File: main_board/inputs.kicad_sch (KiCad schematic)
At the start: 35 parts, among them J16 3.5mm Jack, J17 3.5mm Jack, U10 TLV2172IDR, U11 MCP3021, U12 TLV2172IDR, U13 MCP3021, U15 LM339

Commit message: Ver 2.0 of board.
Also major advances in code.
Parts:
- removed U15: LM339, Package_SO:SOIC-14_3.9x8.7mm_P1.27mm, symbol Comparator:LM339
- added D37, D38: RED LED, LED_THT:LED_D3.0mm, symbol Device:LED
- added R129, R130: 750K, Resistor_SMD:R_0805_2012Metric_Pad1.20x1.40mm_HandSolder, symbol Device:R_Small_US
- added R131, R132: 3.32M, Resistor_SMD:R_0805_2012Metric_Pad1.20x1.40mm_HandSolder, symbol Device:R_Small_US
- added R133, R134, R139, R140: 10K, Resistor_SMD:R_0805_2012Metric_Pad1.20x1.40mm_HandSolder, symbol Device:R_Small_US
- added R135, R136: 2.2K, Resistor_SMD:R_0805_2012Metric_Pad1.20x1.40mm_HandSolder, symbol Device:R_Small_US
- added R137, R138: 1K, Resistor_SMD:R_0805_2012Metric_Pad1.20x1.40mm_HandSolder, symbol Device:R_Small_US
- added U19: TLV2172IDR, Package_SO:SOIC-8-1EP_3.9x4.9mm_P1.27mm_EP2.29x3mm, symbol Amplifier_Operational:TL072
- D19, D20: value RED LED -> BLUE LED; Digi-Key Part 160-1035-ND -> 732-11401-ND
- R38, R39: value 1K -> 1.00M;  LCSC Part # C100047 -> C107700; Digi-Key Part 311-10KARCT-ND -> 311-1.00MCRCT-ND
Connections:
- net +12V: now also R133.1, R134.1, U19.8 (V+); no longer D19.2 (A), D20.2 (A)
- net -12V: now also R139.2, R140.2, U19.4 (V-)
- net GND: now also D19.1 (K), D20.1 (K), D37.2 (A), D38.2 (A), R129.2, R130.2
- net at R36.1, R37.2, U12.1: now also R39.1
- net at R31.1, R32.2, U10.1: now also R38.1
- net at R38.2: now also R131.1, U19.2 (-); no longer D19.1 (K)
- net at R39.2: now also R132.1, U19.6 (-); no longer D20.1 (K)
- new net: D37.1 (K), R137.2, R139.1
- new net: R130.1, U19.5 (+)
- new net: R131.2, R135.1, R137.1, U19.1
- new net: D20.2 (A), R134.2, R136.2
- new net: D19.2 (A), R133.2, R135.2
- new net: R132.2, R136.1, R138.1, U19.7
- new net: D38.1 (K), R138.2, R140.1
- new net: R129.1, U19.3 (+)
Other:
- note added: "Blue"
- note added: "Red"

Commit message: Version 0.03
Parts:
- removed C29: 100nF, Capacitor_SMD:C_0805_2012Metric_Pad1.18x1.45mm_HandSolder, symbol Device:C_Small
- removed U11, U13: MCP3021, Package_TO_SOT_SMD:TSOT-23-5_HandSoldering, symbol greenface:MCP3021
- added SO5, SO6, SO7, SO8: LED_Standoff, symbol greenface:LED_Standoff
- added U11: ADS1015IDGS, Package_SO:TSSOP-10_3x3mm_P0.5mm, symbol Analog_ADC:ADS1015IDGS
- R139, R140: value 10K -> 56K;  LCSC Part # C138260 -> C137420; Digi-Key Part 13-RC0805JR-1010KLCT-ND -> 311-56KARCT-ND
- R28, R33: value 332K .1% -> 30.1K .1%;  LCSC Part # C228750 -> C374678
- R29, R31, R34, R36: value 100K .1% -> 10K .1%;  LCSC Part # C122537 -> C406725; Digi-Key Part YAG1759CT-ND -> (none)
- R30, R35: value 43K -> 4.3K;  LCSC Part # C137429 -> C229218
- U10, U12, U19: value TLV2172IDR -> TL072CDR;  LCSC Part # C129149 -> C67473
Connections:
- net 3.3VRef: now also U11.8 (VDD)
- net GND: now also U11.1 (ADDR), U11.3 (GND)
- net SCL: now also U11.10 (SCL)
- net SDA: now also U11.9 (SDA)
- net at U10.6 (-), U10.7: now also U11.4 (AIN0)
- net at R31.1, R32.2, U10.1: no longer R38.1
- net at R36.1, R37.2, U12.1: no longer R39.1
- net at J16.2 (T), R28.2: now also R38.1
- net at J17.2 (T), R33.2: now also R39.1
- net at U12.6 (-), U12.7: now also U11.5 (AIN1)
- new net +1.65V: U11.7 (AIN3)
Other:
- moved on the sheet: C25, D19, D20, D37, D38, R129, R130, R131, R132, R133, R134, R135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

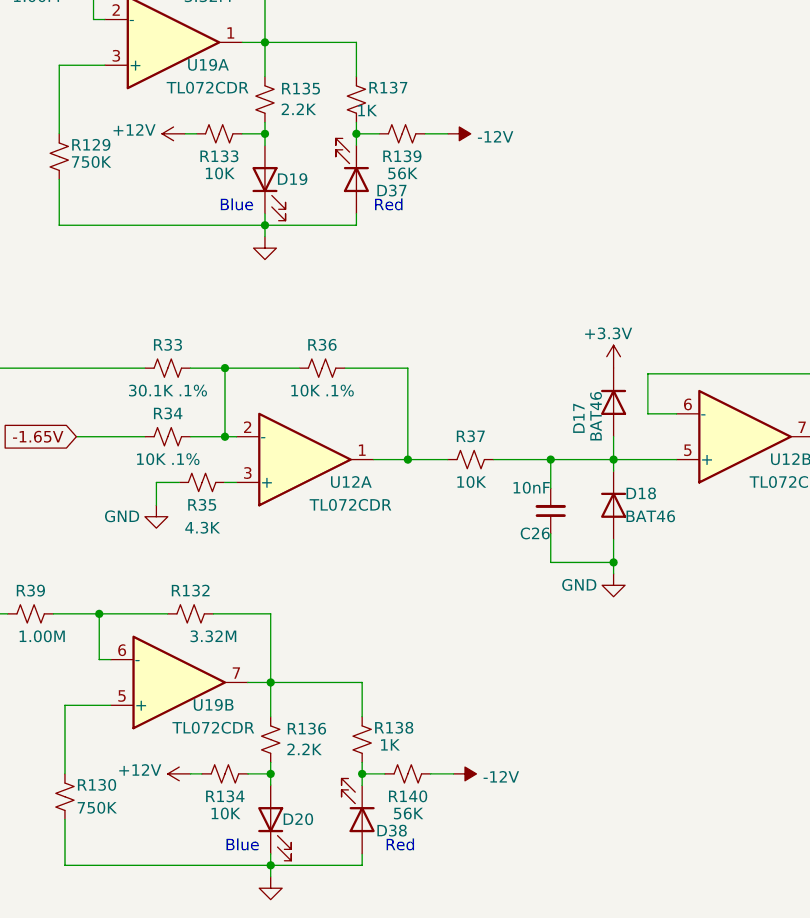
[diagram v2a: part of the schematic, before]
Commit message: Software v2.2
Removes unneeded files.
Adds pre-flight handler in WiFi do_server();
Removes debug printouts.
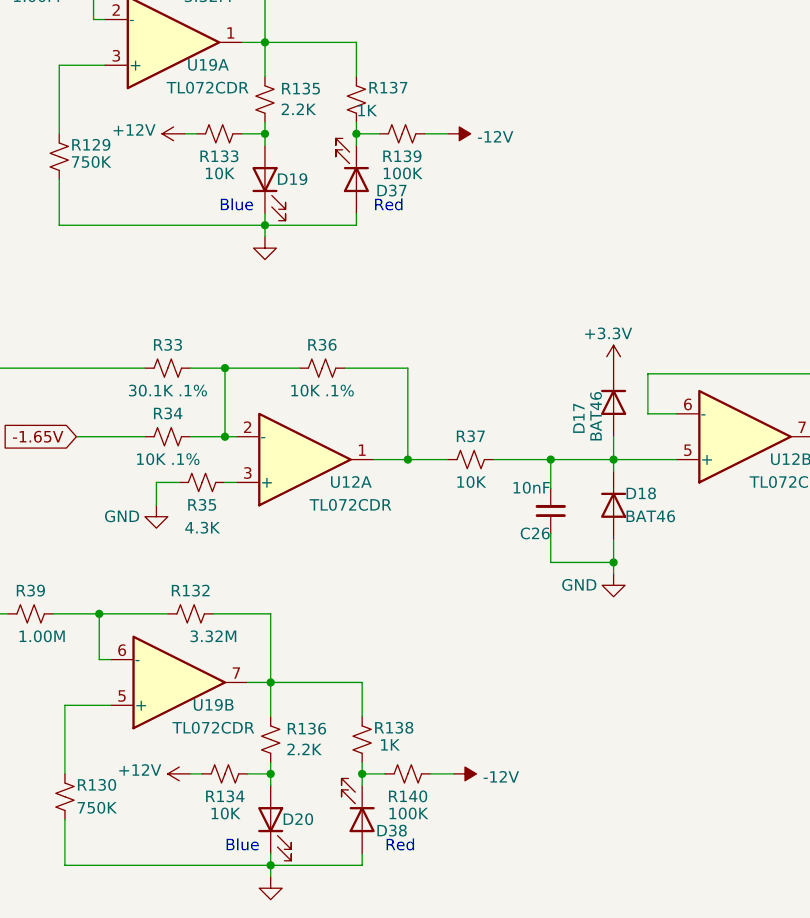
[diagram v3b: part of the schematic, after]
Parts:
- R139, R140: value 56K -> 100K;  LCSC Part # C137420 -> C100049
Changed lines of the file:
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@@
     (in_bom yes) (on_board yes)
     (property "Reference" "R139" (id 0) (at 127 83.82 90))
-    (property "Value" "56K" (id 1) (at 127 85.725 90))
+    (property "Value" "100K" (id 1) (at 127 85.725 90))
     (property "Footprint" "Resistor_SMD:R_0805_2012Metric_Pad1.20x1.40mm_HandSolder" (id 2) (at 127 81.28 0)
       (effects (font (size 1.27 1.27)) hide)
@@
       (effects (font (size 1.27 1.27)) hide)
     )
-    (property " LCSC Part #" "C137420" (id 5) (at 127 81.28 0)
+    (property " LCSC Part #" "C100049" (id 5) (at 127 81.28 0)
       (effects (font (size 1.27 1.27)) hide)
     )
@@
     (in_bom yes) (on_board yes)
     (property "Reference" "R140" (id 0) (at 127.635 154.94 90))
-    (property "Value" "56K" (id 1) (at 127.635 156.845 90))
+    (property "Value" "100K" (id 1) (at 127.635 156.845 90))
     (property "Footprint" "Resistor_SMD:R_0805_2012Metric_Pad1.20x1.40mm_HandSolder" (id 2) (at 127.635 152.4 0)
       (effects (font (size 1.27 1.27)) hide)
@@
       (effects (font (size 1.27 1.27)) hide)
     )
-    (property " LCSC Part #" "C137420" (id 5) (at 127.635 152.4 0)
-      (effects (font (size 1.27 1.27)) hide)
-    )
+    (property " LCSC Part #" "C100049" (id 5) (at 127.635 152.4 0)
+      (effects (font (size 1.27 1.27)) hide)
+    )

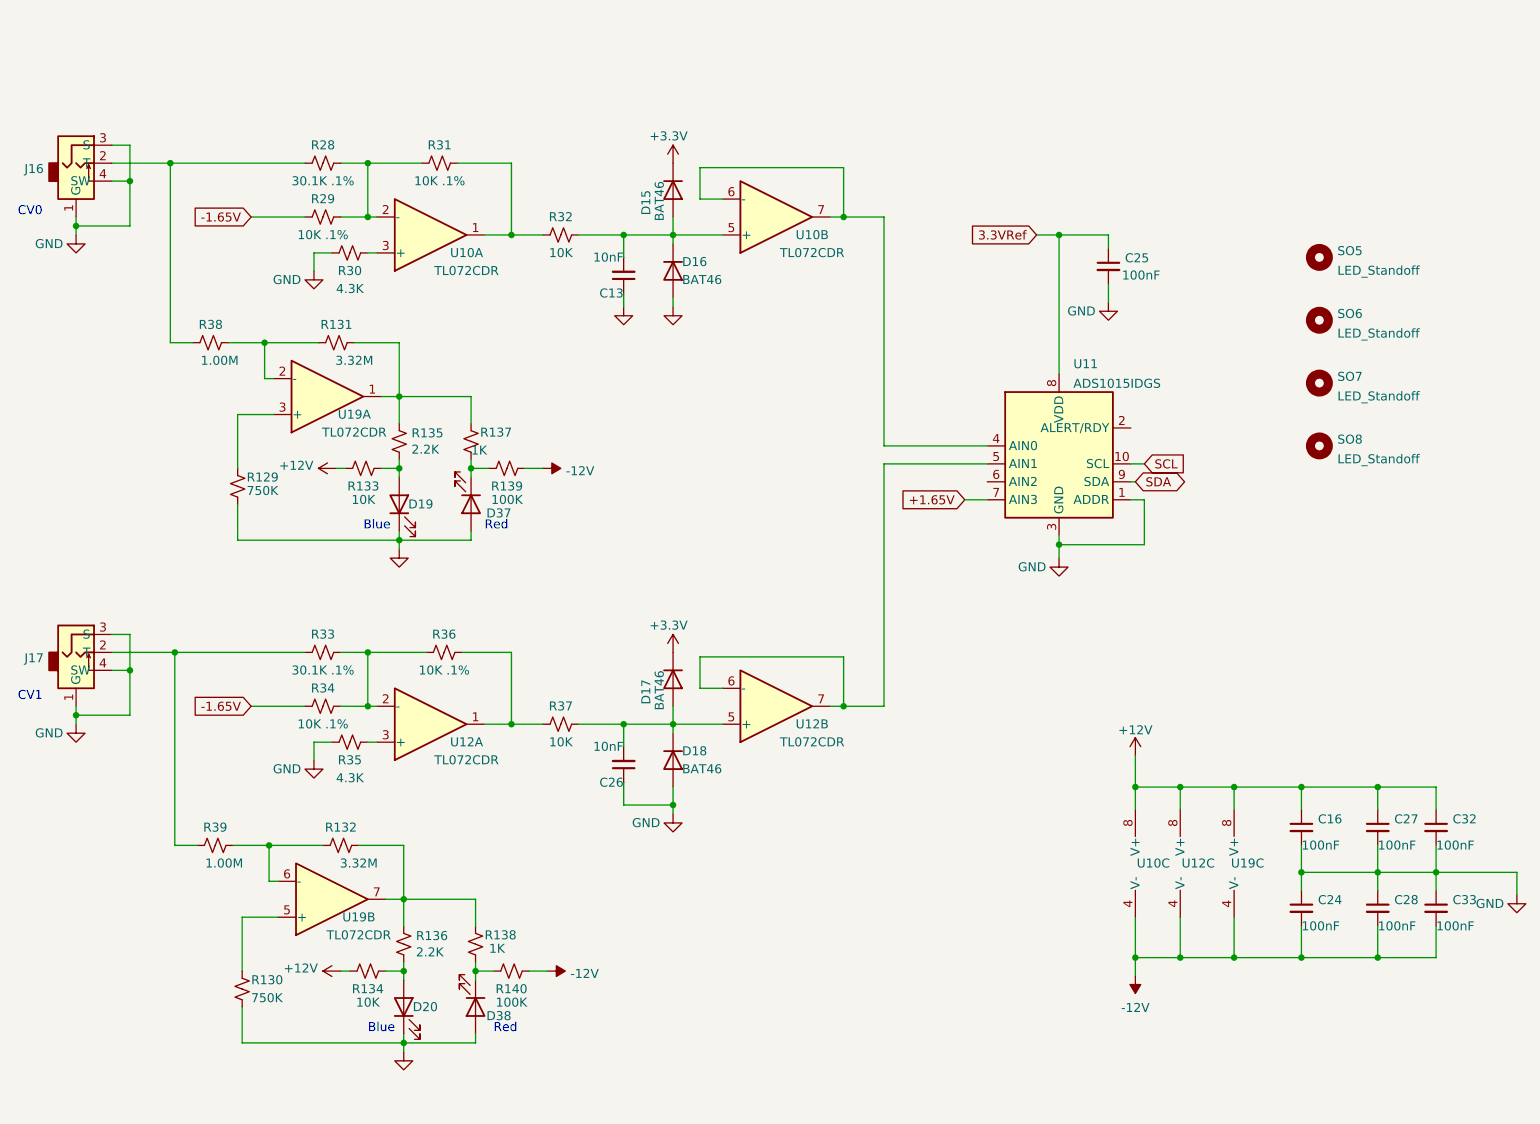
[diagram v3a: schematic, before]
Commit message: Updates monitor circuitry. Sets outputs on init().
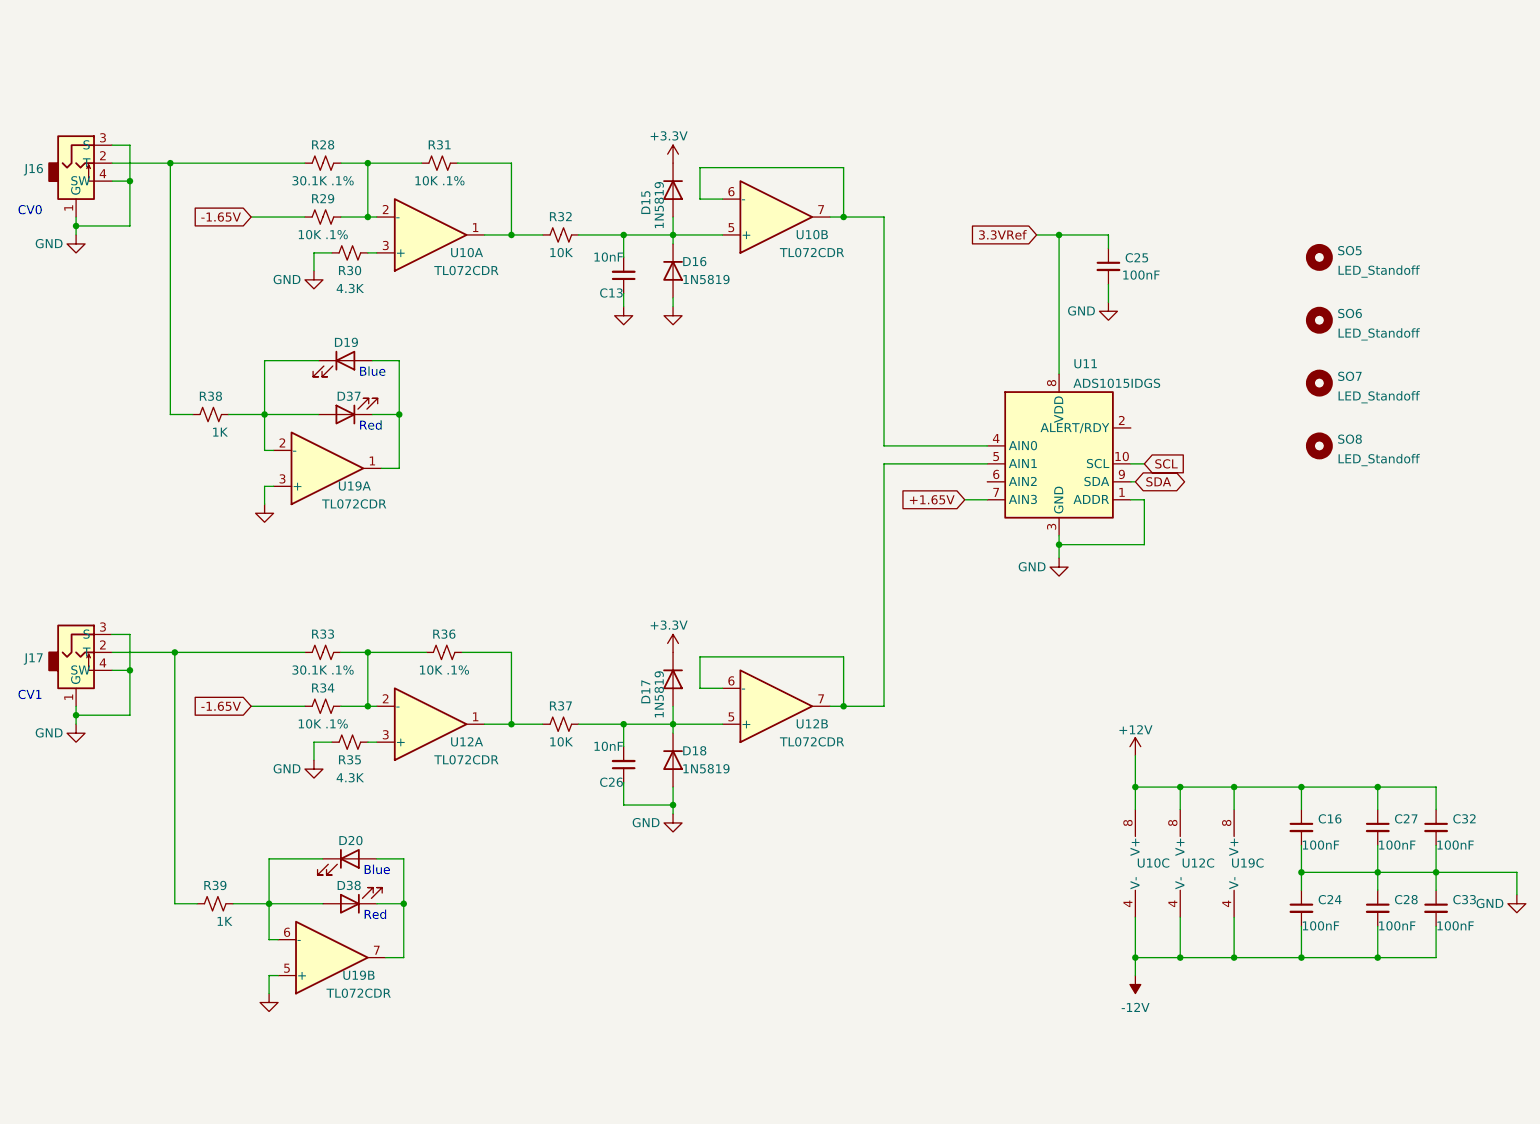
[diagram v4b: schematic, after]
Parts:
- removed R129, R130: 750K, Resistor_SMD:R_0805_2012Metric_Pad1.20x1.40mm_HandSolder, symbol Device:R_Small_US
- removed R131, R132: 3.32M, Resistor_SMD:R_0805_2012Metric_Pad1.20x1.40mm_HandSolder, symbol Device:R_Small_US
- removed R133, R134: 10K, Resistor_SMD:R_0805_2012Metric_Pad1.20x1.40mm_HandSolder, symbol Device:R_Small_US
- removed R135, R136: 2.2K, Resistor_SMD:R_0805_2012Metric_Pad1.20x1.40mm_HandSolder, symbol Device:R_Small_US
- removed R137, R138: 1K, Resistor_SMD:R_0805_2012Metric_Pad1.20x1.40mm_HandSolder, symbol Device:R_Small_US
- removed R139, R140: 100K, Resistor_SMD:R_0805_2012Metric_Pad1.20x1.40mm_HandSolder, symbol Device:R_Small_US
- C13, C26:  LCSC Part # C83170 -> C1710
- D15, D16, D17, D18: value BAT46 -> 1N5819;  LCSC Part # C123899 -> C191023
- R30, R35:  LCSC Part # C229218 -> C17667
- R32, R37:  LCSC Part # C138260 -> C17414
- R38, R39: value 1.00M -> 1K;  LCSC Part # C107700 -> C17513; Digi-Key Part 311-1.00MCRCT-ND -> 311-10KARCT-ND
- U10, U12, U19:  LCSC Part # C67473 -> C6961
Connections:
- net GND: now also U19.3 (+), U19.5 (+); no longer D19.1 (K), D20.1 (K), D37.2 (A), D38.2 (A)
- net at R38.2, U19.2 (-): now also D19.1 (K), D37.2 (A)
- net at D37.1 (K): now also D19.2 (A), U19.1
- net at R39.2, U19.6 (-): now also D20.1 (K), D38.2 (A)
- net at D20.2 (A): now also D38.1 (K), U19.7
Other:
- moved on the sheet: D19, D20, D37, D38, R38, R39, U19A, U19B

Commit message: Upgrades board to v5. Adds Bonk Daddy.
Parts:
- added D39, D40, D41, D42: 1N5819, Diode_SMD:D_0805_2012Metric_Pad1.15x1.40mm_HandSolder, symbol Diode:1N4148
- added R56, R57: 10K, Resistor_SMD:R_0805_2012Metric_Pad1.20x1.40mm_HandSolder, symbol Device:R_Small_US
- U19: footprint Package_SO:SOIC-8-1EP_3.9x4.9mm_P1.27mm_EP2.29x3mm -> Package_SO:SOIC-8_3.9x4.9mm_P1.27mm
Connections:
- net +12V: now also D39.1 (K), D41.1 (K)
- net -12V: now also D40.2 (A), D42.2 (A)
- net GND: now also R38.1, R39.1; no longer U19.3 (+), U19.5 (+)
- net at J16.2 (T), R28.2: now also R56.1; no longer R38.1
- net at R38.2, U19.2 (-): now also D19.2 (A), D37.1 (K); no longer D19.1 (K), D37.2 (A)
- net at J17.2 (T), R33.2: now also R57.1; no longer R39.1
- net at R39.2, U19.6 (-): now also D20.2 (A), D38.1 (K); no longer D20.1 (K), D38.2 (A)
- new net: D41.2 (A), D42.1 (K), R57.2, U19.5 (+)
- new net: D39.2 (A), D40.1 (K), R56.2, U19.3 (+)
- new net: D19.1 (K), D37.2 (A), U19.1
- new net: D20.1 (K), D38.2 (A), U19.7
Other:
- moved on the sheet: D19, D20, D37, D38, R38, R39, U19A, U19B

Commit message: LED current resistors now 2,.2K
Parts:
- R38, R39: value 1K -> 2.2K;  LCSC Part # C17513 -> C17520
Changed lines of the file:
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@@
     (in_bom yes) (on_board yes)
     (property "Reference" "R38" (id 0) (at 100.33 71.12 90))
-    (property "Value" "1K" (id 1) (at 101.6 76.2 90))
+    (property "Value" "2.2K" (id 1) (at 101.6 76.2 90))
     (property "Footprint" "Resistor_SMD:R_0805_2012Metric_Pad1.20x1.40mm_HandSolder" (id 2) (at 100.33 73.66 0)
       (effects (font (size 1.27 1.27)) hide)
@@
       (effects (font (size 1.27 1.27)) hide)
     )
-    (property " LCSC Part #" "C17513" (id 5) (at 100.33 73.66 0)
+    (property " LCSC Part #" "C17520" (id 5) (at 100.33 73.66 0)
       (effects (font (size 1.27 1.27)) hide)
     )
@@
     (in_bom yes) (on_board yes)
     (property "Reference" "R39" (id 0) (at 101.6 140.335 90))
-    (property "Value" "1K" (id 1) (at 102.87 145.415 90))
+    (property "Value" "2.2K" (id 1) (at 102.87 145.415 90))
     (property "Footprint" "Resistor_SMD:R_0805_2012Metric_Pad1.20x1.40mm_HandSolder" (id 2) (at 101.6 142.875 0)
       (effects (font (size 1.27 1.27)) hide)
@@
       (effects (font (size 1.27 1.27)) hide)
     )
-    (property " LCSC Part #" "C17513" (id 5) (at 101.6 142.875 0)
-      (effects (font (size 1.27 1.27)) hide)
-    )
+    (property " LCSC Part #" "C17520" (id 5) (at 101.6 142.875 0)
+      (effects (font (size 1.27 1.27)) hide)
+    )

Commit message: Updates main_board, uses generate_boms.bat
Updates reverse protection circuitry on main board.
Updates 3.3V reference circuitry.
Uses generate_boms and retires .xlsx BOM files.
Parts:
- C13, C26:  LCSC Part # C1710 -> (none); LCSC Part # (none) -> C1710
- C16, C24, C25, C27, C28, C32, C33:  LCSC Part # C49678 -> (none); LCSC Part # (none) -> C49678
- D15, D16, D17, D18, D39, D40, D41, D42:  LCSC Part # C191023 -> (none); LCSC Part # (none) -> C191023
- R28, R33:  LCSC Part # C374678 -> (none); LCSC Part # (none) -> C374678
- R29, R31, R34, R36:  LCSC Part # C406725 -> (none); LCSC Part # (none) -> C406725
- R30, R35:  LCSC Part # C17667 -> (none); LCSC Part # (none) -> C17667
- R32, R37, R56, R57:  LCSC Part # C17414 -> (none); LCSC Part # (none) -> C17414
- R38, R39:  LCSC Part # C17520 -> (none); LCSC Part # (none) -> C17520
- U10, U12, U19:  LCSC Part # C6961 -> (none); LCSC Part # (none) -> C6961
- U11:  LCSC Part # C193969 -> (none); LCSC Part # (none) -> C193969
